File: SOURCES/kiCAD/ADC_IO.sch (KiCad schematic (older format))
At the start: 154 parts, among them IC2 PCM1808QPWRQ1, J1 Conn_01x08, J11 Conn_Coaxial, J12 IDC_2x5, J3 Conn_01x08, J5 Conn_Coaxial_x2, J6 8P_DIP_SOCKET, Q12 MJD45H11T4, Q13 2N7002, Q29 AO3401A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

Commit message: Updated version0.2
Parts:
- J11, J12: JLPCB# NOP -> HAND
- JP2: value Jumper_NO -> Jumper_NC; footprint Jumper:SolderJumper-2_P1.3mm_Open_RoundedPad1.0x1.5mm -> Jumper:SolderJumper-2_P1.3mm_Bridged_RoundedPad1.0x1.5mm; symbol Device:Jumper_NO_Small -> Device:Jumper_NC_Small
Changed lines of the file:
@@
 F 2 "Connector_IDC:IDC-Header_2x05_P2.54mm_Horizontal" H 7150 10000 60  0001 C CNN
 F 3 "" H 7175 8850 60  0000 C CNN
-F 4 "NOP" H 7175 10050 50  0001 C CNN "JLPCB#"
+F 4 "HAND" H 7175 10050 50  0001 C CNN "JLPCB#"
 	1    7175 10050
 	1    0    0    -1
@@
 $EndComp
 $Comp
-L Device:Jumper_NO_Small JP2
+L Device:Jumper_NC_Small JP2
 U 1 1 670E4F79
 P 4500 1675
 F 0 "JP2" H 4500 1600 50  0000 C CNN
-F 1 "Jumper_NO" H 4600 1725 50  0000 C CNN
-F 2 "Jumper:SolderJumper-2_P1.3mm_Open_RoundedPad1.0x1.5mm" H 4500 1675 50  0001 C CNN
+F 1 "Jumper_NC" H 4550 1825 50  0000 C CNN
+F 2 "Jumper:SolderJumper-2_P1.3mm_Bridged_RoundedPad1.0x1.5mm" H 4500 1675 50  0001 C CNN
 F 3 "~" H 4500 1675 50  0001 C CNN
 F 4 "NOP" H 4500 1675 50  0001 C CNN "JLPCB#"
@@
 F 2 "MyJacks:RJ-2410N" H 1250 10475 50  0001 C CNN
 F 3 " ~" H 1250 10475 50  0001 C CNN
-F 4 "NOP" H 1250 10475 50  0001 C CNN "JLPCB#"
+F 4 "HAND" H 1250 10475 50  0001 C CNN "JLPCB#"
 	1    1250 10475
 	-1   0    0    -1

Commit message: version 0.2 updates
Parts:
- U13: value 25LC_1024 -> 24AA1024
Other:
- note added: "NOTE:\nEEPROM page-size should be 8 (8x128k, 8x32k, etc..)\n BR25G1MF-3GE2(ROHM)\n CAT25M01VI-GT3(OnSemi)\n M95M01-DWMN3TP/K(STM)\n S-25CM01A0I-J8T1U4(ablic)\n\nRemove U13 when use a J6 DIP package EEPROM.\nRemove R43 when you install the SW4 for selectable dual EEPROMs."
- note removed: "NOTE:\nRemove U13 when use the J6 DIP package EEPROMs."
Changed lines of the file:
@@
 Sheet 2 3
 Title "FreeDSP OCTAVIA ADC/DSP Part"
-Date "2023-03-11"
-Rev "0.2"
+Date "2023-04-15"
+Rev "0.21"
 Comp ""
 Comment1 ""
@@
 P 8650 7500
 F 0 "U13" H 8925 7750 50  0000 C CNN
-F 1 "25LC_1024" H 8375 7250 50  0000 C CNN
+F 1 "24AA1024" H 8375 7250 50  0000 C CNN
 F 2 "Package_SO:SOIC-8_5.275x5.275mm_P1.27mm" H 8300 7450 50  0001 C CNN
 F 3 "http://ww1.microchip.com/downloads/en/DeviceDoc/21832H.pdf" H 8625 7900 50  0001 C CNN
@@
 Wire Notes Line
 	8925 8175 8400 8175
-Text Notes 10075 8475 0    79   ~ 16
+Text Notes 10125 7100 0    79   ~ 16
 OPTIONAL\nSOCKET
 Wire Notes Line
-	10075 8200 10075 8500
+	10125 6825 10125 7125
 Wire Notes Line
-	10100 8500 10650 8500
+	10150 7125 10700 7125
 Wire Notes Line
-	10650 8500 10650 8200
+	10700 7125 10700 6825
 Wire Notes Line
-	10650 8200 10100 8200
-Text Notes 8825 8025 0    50   ~ 0
-NOTE:\nRemove U13 when use the J6 DIP package EEPROMs.
+	10700 6825 10150 6825
+Text Notes 9000 8575 0    50   ~ 0
+NOTE:\nEEPROM page-size should be 8 (8x128k, 8x32k, etc..)\n    BR25G1MF-3GE2(ROHM)\n    CAT25M01VI-GT3(OnSemi)\n    M95M01-DWMN3TP/K(STM)\n    S-25CM01A0I-J8T1U4(ablic)\n\nRemove U13 when use a J6 DIP package EEPROM.\nRemove R43 when you install the SW4 for selectable dual EEPROMs.
 $Comp
 L Device:R R?

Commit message: version 0.2 updates
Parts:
- U13: value 24AA1024 -> 25AA1024
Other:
- note added: "NOTE:\nRemove U13 when use a J6 DIP package EEPROM.\nRemove R43 when you install the SW4 for selectable dual EEPROMs.\n\nSPI EEPROM should be organized by 8 (128kx8, 64kx8, 32kx8, etc.. )\nThe maximum valid memory space is limited up to 512Mbits.\nMaybe you can replace U13 EEPROM with following lists…\n 25AA1024-I/SM(Microchip, Evaluated)\n BR25G1MF-3GE2(ROHM)\n CAT25M01VI-GT3(OnSemi)\n S-25CM01A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"
- note removed: "NOTE:\nEEPROM page-size should be 8 (8x128k, 8x32k, etc..)\n BR25G1MF-3GE2(ROHM)\n CAT25M01VI-GT3(OnSemi)\n M95M01-DWMN3TP/K(STM)\n S-25CM01A0I-J8T1U4(ablic)\n\nRemove U13 when use a J6 DIP package EEPROM.\nRemove R43 when you install the SW4 for selectable dual EEPROMs."
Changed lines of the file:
@@
 P 8650 7500
 F 0 "U13" H 8925 7750 50  0000 C CNN
-F 1 "24AA1024" H 8375 7250 50  0000 C CNN
+F 1 "25AA1024" H 8375 7250 50  0000 C CNN
 F 2 "Package_SO:SOIC-8_5.275x5.275mm_P1.27mm" H 8300 7450 50  0001 C CNN
 F 3 "http://ww1.microchip.com/downloads/en/DeviceDoc/21832H.pdf" H 8625 7900 50  0001 C CNN
@@
 Wire Notes Line
 	10700 6825 10150 6825
-Text Notes 9000 8575 0    50   ~ 0
-NOTE:\nEEPROM page-size should be 8 (8x128k, 8x32k, etc..)\n    BR25G1MF-3GE2(ROHM)\n    CAT25M01VI-GT3(OnSemi)\n    M95M01-DWMN3TP/K(STM)\n    S-25CM01A0I-J8T1U4(ablic)\n\nRemove U13 when use a J6 DIP package EEPROM.\nRemove R43 when you install the SW4 for selectable dual EEPROMs.
-$Comp
-L Device:R R?
+Text Notes 9000 8850 0    50   ~ 0
+NOTE:\nRemove U13 when use a J6 DIP package EEPROM.\nRemove R43 when you install the SW4 for selectable dual EEPROMs.\n\nSPI EEPROM should be organized by 8 (128kx8, 64kx8, 32kx8, etc.. )\nThe maximum valid memory space is limited up to 512Mbits.\nMaybe you can replace U13 EEPROM with following lists…\n    25AA1024-I/SM(Microchip, Evaluated)\n    BR25G1MF-3GE2(ROHM)\n    CAT25M01VI-GT3(OnSemi)\n    S-25CM01A0I-J8T1U4(ablic)\n    M95M01-DWMN3TP/K(STM)\n
+$Comp
+L Device:R R?

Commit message: Version0.2 Board. Reviced PCB design.
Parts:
- removed R49: 3.3k, Resistor_SMD:R_0603_1608Metric, symbol Device:R
- added J10, J9: Conn_01x02, Connector_PinHeader_2.54mm:PinHeader_1x02_P2.54mm_Vertical, symbol Connector_Generic:Conn_01x02
- C27, C28: Description (none) -> Audio Grade Cap Recommended
- D17, D18: Description (none) -> Remove this if you use extension header
- IC2: Description Automotive 99dB SNR Stereo ADC With Single-Ended Inputs -> 99dB SNR is only for 48kHz Sampling
- J1: Description (none) -> for Optinal Extension of POTs
- J11: Description (none) -> RCA-pin Input Connector
- J12: Description (none) -> for USBi
- J3: Description (none) -> for Optional I2S-1 Input
- J5: value Conn_Coaxial_x2 -> MJ-519; JLPCB# NOP -> HAND
- J6: Description (none) -> Just for the Altanative choice of EEPROM package
- JP1: Description (none) -> Prevent Selfboot if shorted
- JP2: Description (none) -> Cut for 96kHz A/D Convertion
- R76: value 3.3k -> 330R; JLPCB# C22978 -> C17630
- R92, R94: value 100 -> 100R
- SW7: footprint OPL_Switch:SW2-5.0-6.0X3.0X4.3MM -> Button_Switch_THT:SW_Tactile_SPST_Angled_PTS645Vx83-2LFS; Description (none) -> for manual reset button for DSP
- U10: JLPCB# C402161 -> C73458
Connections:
- net +3V3: now also J10.2 (Pin_2), J9.2 (Pin_2)
- net at D18.1 (K), R98.1: now also J10.1 (Pin_1)
- net at D17.1 (K), R96.1: now also J9.1 (Pin_1)
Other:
- note added: "(-0.5dB)"
- note added: "ANODE\nCATHODE"
- note added: "EXT"
- note added: "NOTE:\nRemove U13 when use a J6 DIP package instead of SOIC package EEPROM.\nRemove R43 when you install the SW4 for selectable dual EEPROMs.\n\nSPI EEPROM should be organized by 8 (128kx8, 64kx8, 32kx8, etc.. )\nThe maximum valid memory space is limited up to 512Mbits.\nMaybe you can replace U13 EEPROM which contained in the following lists, but you need to change the writting parameters…\n\n 25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"
- note added: "RCA"
- note added: "RPI"
- note added: "USB"
- note removed: "(-1dB)"
- note removed: "NOTE:\nRemove U13 when use a J6 DIP package EEPROM.\nRemove R43 when you install the SW4 for selectable dual EEPROMs.\n\nSPI EEPROM should be organized by 8 (128kx8, 64kx8, 32kx8, etc.. )\nThe maximum valid memory space is limited up to 512Mbits.\nMaybe you can replace U13 EEPROM with following lists…\n 25AA1024-I/SM(Microchip, Evaluated)\n BR25G1MF-3GE2(ROHM)\n CAT25M01VI-GT3(OnSemi)\n S-25CM01A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"
- moved on the sheet: D17, D18, R96, R98

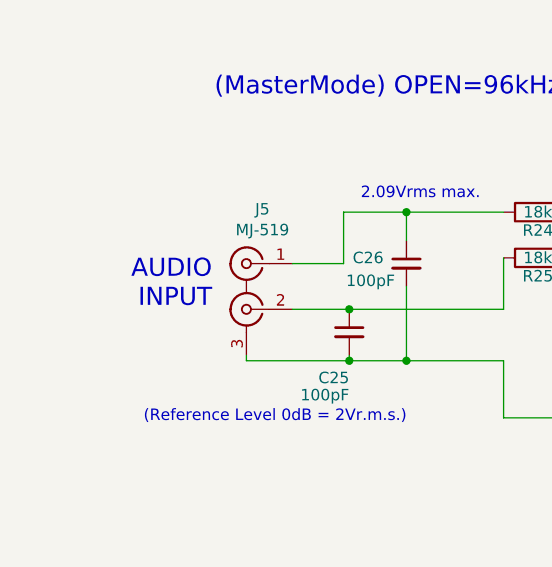
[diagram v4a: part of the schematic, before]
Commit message: Fixed wrong L/R Connection of RCA Jack
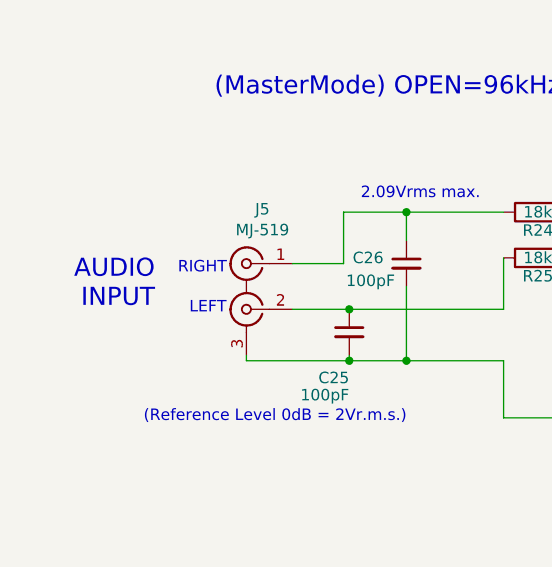
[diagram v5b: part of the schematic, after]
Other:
- note added: "LEFT"
- note added: "RIGHT"
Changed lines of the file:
@@
 Text Notes 3675 925  2    79   ~ 0
 (MasterMode) OPEN=96kHz, SHORT=48kHz
-Text Notes 1275 1850 2    79   ~ 0
+Text Notes 1025 1850 2    79   ~ 0
 AUDIO\nINPUT
 $Comp
@@
 Text Notes 12525 8925 2    63   ~ 0
 ANODE\nCATHODE
+Text Notes 1125 1700 0    50   ~ 0
+RIGHT
+Text Notes 1175 1875 0    50   ~ 0
+LEFT
 $EndSCHEMATC

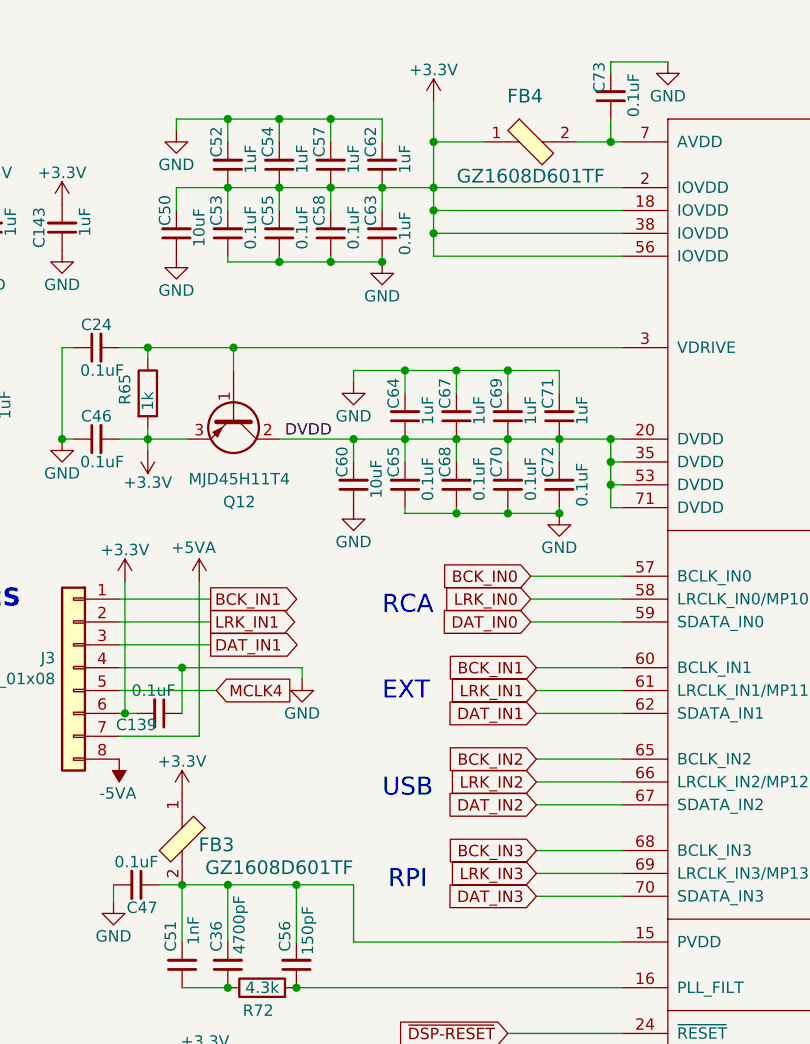
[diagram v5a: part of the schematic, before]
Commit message: New Output Driver with Enhanced 4 Layer PCB
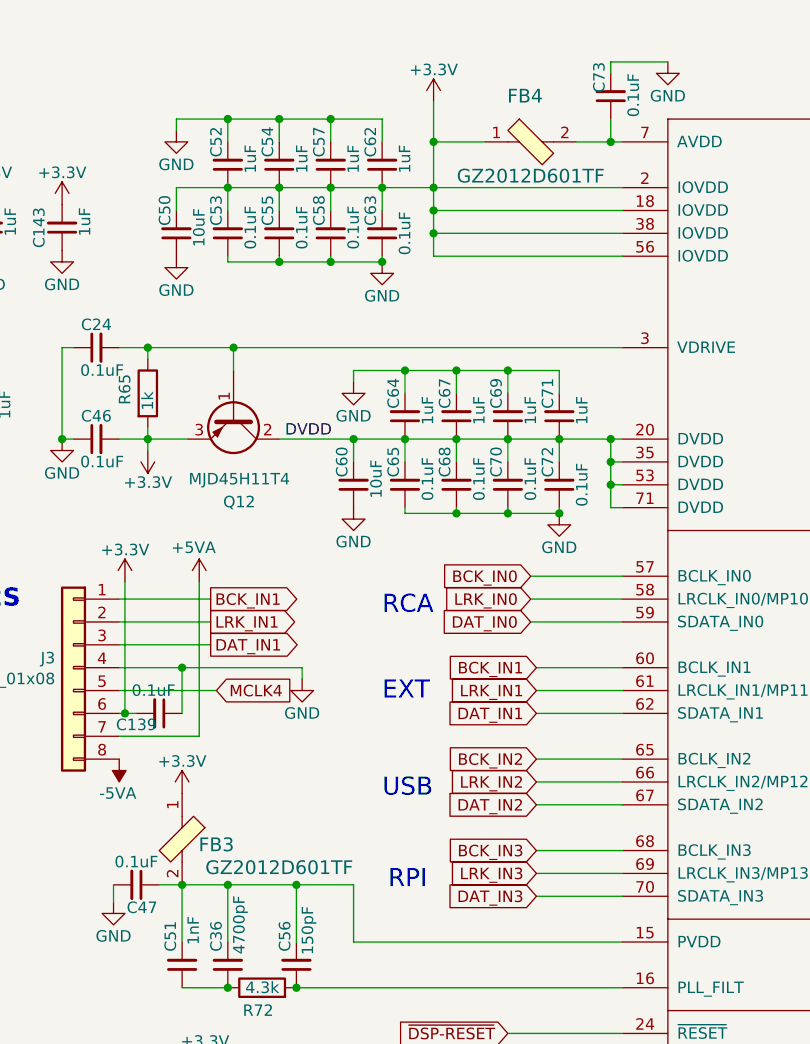
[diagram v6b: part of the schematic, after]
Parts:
- FB3, FB4: value GZ1608D601TF -> GZ2012D601TF; footprint digikey-footprints:0603 -> digikey-footprints:0805; Description FERRITE BEAD 600 OHM 0603 1LN -> FERRITE BEAD 600 OHM; JLPCB# C1002 -> C1017
- J5: footprint MyCompo:MJ-519 -> MyJacks:MJ-519
- T1: footprint PE65612NL -> MyLibrary:PE65612NL
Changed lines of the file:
@@
 Sheet 2 3
 Title "FreeDSP OCTAVIA ADC/DSP Part"
-Date "2023-05-13"
-Rev "0.25"
+Date "2023-07-22"
+Rev "0.3"
 Comp ""
 Comment1 ""
@@
 F 0 "J5" H 1355 2088 50  0000 C CNN
 F 1 "MJ-519" H 1355 1997 50  0000 C CNN
-F 2 "MyCompo:MJ-519" H 1425 1650 50  0001 C CNN
+F 2 "MyJacks:MJ-519" H 1425 1650 50  0001 C CNN
 F 3 " ~" H 1425 1650 50  0001 C CNN
 F 4 "HAND" H 1425 1750 50  0001 C CNN "JLPCB#"
@@
 P 3600 3600
 F 0 "FB4" H 3575 3800 60  0000 C CNN
-F 1 "GZ1608D601TF" H 3600 3450 60  0000 C CNN
-F 2 "digikey-footprints:0603" H 3800 3800 60  0001 L CNN
+F 1 "GZ2012D601TF " H 3600 3450 60  0000 C CNN
+F 2 "digikey-footprints:0805" H 3800 3800 60  0001 L CNN
 F 3 "https://www.murata.com/en-us/products/productdata/8796738650142/ENFA0003.pdf" H 3800 3900 60  0001 L CNN
 F 4 "490-1014-1-ND" H 3800 4000 60  0001 L CNN "Digi-Key_PN"
@@
 F 8 "https://www.murata.com/en-us/products/productdata/8796738650142/ENFA0003.pdf" H 3800 4400 60  0001 L CNN "DK_Datasheet_Link"
 F 9 "/product-detail/en/murata-electronics-north-america/BLM18AG601SN1D/490-1014-1-ND/584462" H 3800 4500 60  0001 L CNN "DK_Detail_Page"
-F 10 "FERRITE BEAD 600 OHM 0603 1LN" H 3800 4600 60  0001 L CNN "Description"
+F 10 "FERRITE BEAD 600 OHM" H 3800 4600 60  0001 L CNN "Description"
 F 11 "Murata Electronics North America" H 3800 4700 60  0001 L CNN "Manufacturer"
 F 12 "Active" H 3800 4800 60  0001 L CNN "Status"
-F 13 "C1002" H 3600 3600 50  0001 C CNN "JLPCB#"
+F 13 "C1017" H 3600 3600 50  0001 C CNN "JLPCB#"
 	1    3600 3600
 	1    0    0    -1
@@
 P 2075 6650
 F 0 "FB3" V 2100 6800 60  0000 C CNN
-F 1 "GZ1608D601TF" V 2200 7075 60  0000 C CNN
-F 2 "digikey-footprints:0603" H 2275 6850 60  0001 L CNN
+F 1 "GZ2012D601TF " V 2200 7075 60  0000 C CNN
+F 2 "digikey-footprints:0805" H 2275 6850 60  0001 L CNN
 F 3 "https://www.murata.com/en-us/products/productdata/8796738650142/ENFA0003.pdf" H 2275 6950 60  0001 L CNN
 F 4 "490-1014-1-ND" H 2275 7050 60  0001 L CNN "Digi-Key_PN"
@@
 F 8 "https://www.murata.com/en-us/products/productdata/8796738650142/ENFA0003.pdf" H 2275 7450 60  0001 L CNN "DK_Datasheet_Link"
 F 9 "/product-detail/en/murata-electronics-north-america/BLM18AG601SN1D/490-1014-1-ND/584462" H 2275 7550 60  0001 L CNN "DK_Detail_Page"
-F 10 "FERRITE BEAD 600 OHM 0603 1LN" H 2275 7650 60  0001 L CNN "Description"
+F 10 "FERRITE BEAD 600 OHM" H 2275 7650 60  0001 L CNN "Description"
 F 11 "Murata Electronics North America" H 2275 7750 60  0001 L CNN "Manufacturer"
 F 12 "Active" H 2275 7850 60  0001 L CNN "Status"
-F 13 "C1002" H 2075 6650 50  0001 C CNN "JLPCB#"
+F 13 "C1017" H 2075 6650 50  0001 C CNN "JLPCB#"
 	1    2075 6650
 	0    1    1    0
@@
 F 0 "T1" H 1950 10775 50  0000 C CNN
 F 1 "PE-65612NL" H 1950 10675 50  0000 C CNN
-F 2 "PE65612NL" H 2200 10575 50  0001 L CNN
+F 2 "MyLibrary:PE65612NL" H 2200 10575 50  0001 L CNN
 F 3 "https://componentsearchengine.com/Datasheets/1/PE-65612NL.pdf" H 2200 10475 50  0001 L CNN
 F 4 "Audio Transformers / Signal Transformers THT Digital Audio 2500uH 1-Port" H 2200 10375 50  0001 L CNN "Description"
